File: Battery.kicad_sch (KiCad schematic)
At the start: 0 parts

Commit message: added li-pol input, start creating charging circuit
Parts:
- added J4: B2B-PH-K-S, Connector_JST:JST_PH_B2B-PH-K_1x02_P2.00mm_Vertical, symbol 0_connectors:B2B-PH-K-S
- added J5: B3B-PH-K-S, Connector_JST:JST_PH_B3B-PH-K_1x03_P2.00mm_Vertical, symbol 0_connectors:B3B-PH-K-S
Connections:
- new net +BATT: J4.1 (Pin_1), J5.1 (Pin_1)
- new net GND: J4.2 (Pin_2), J5.2 (Pin_2)
- new net NTC_BATT: J5.3 (Pin_2)
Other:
- title: (none) -> Power - Battery

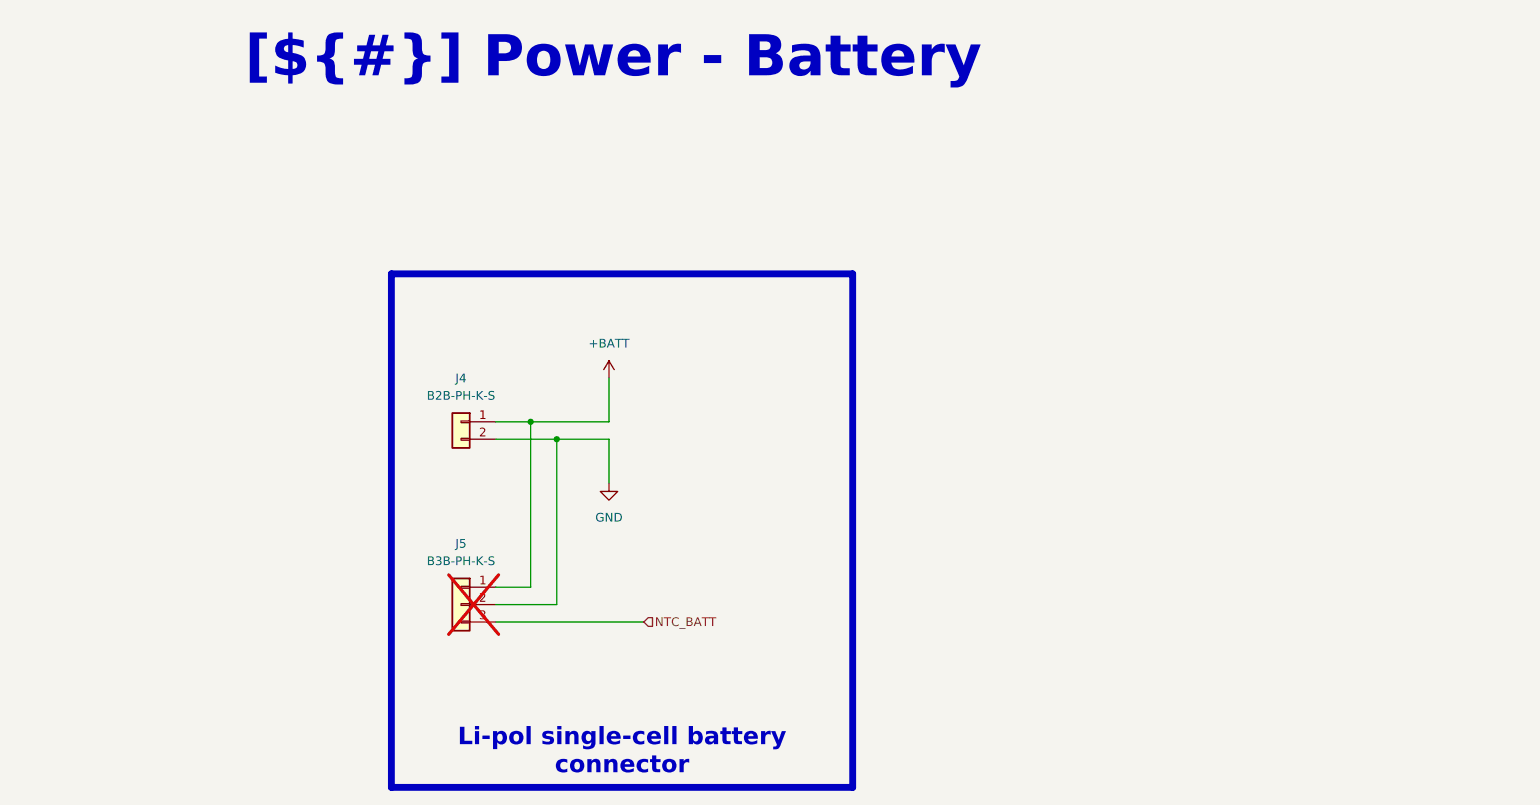
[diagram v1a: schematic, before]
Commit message: added gas guage IC for monitoring battery
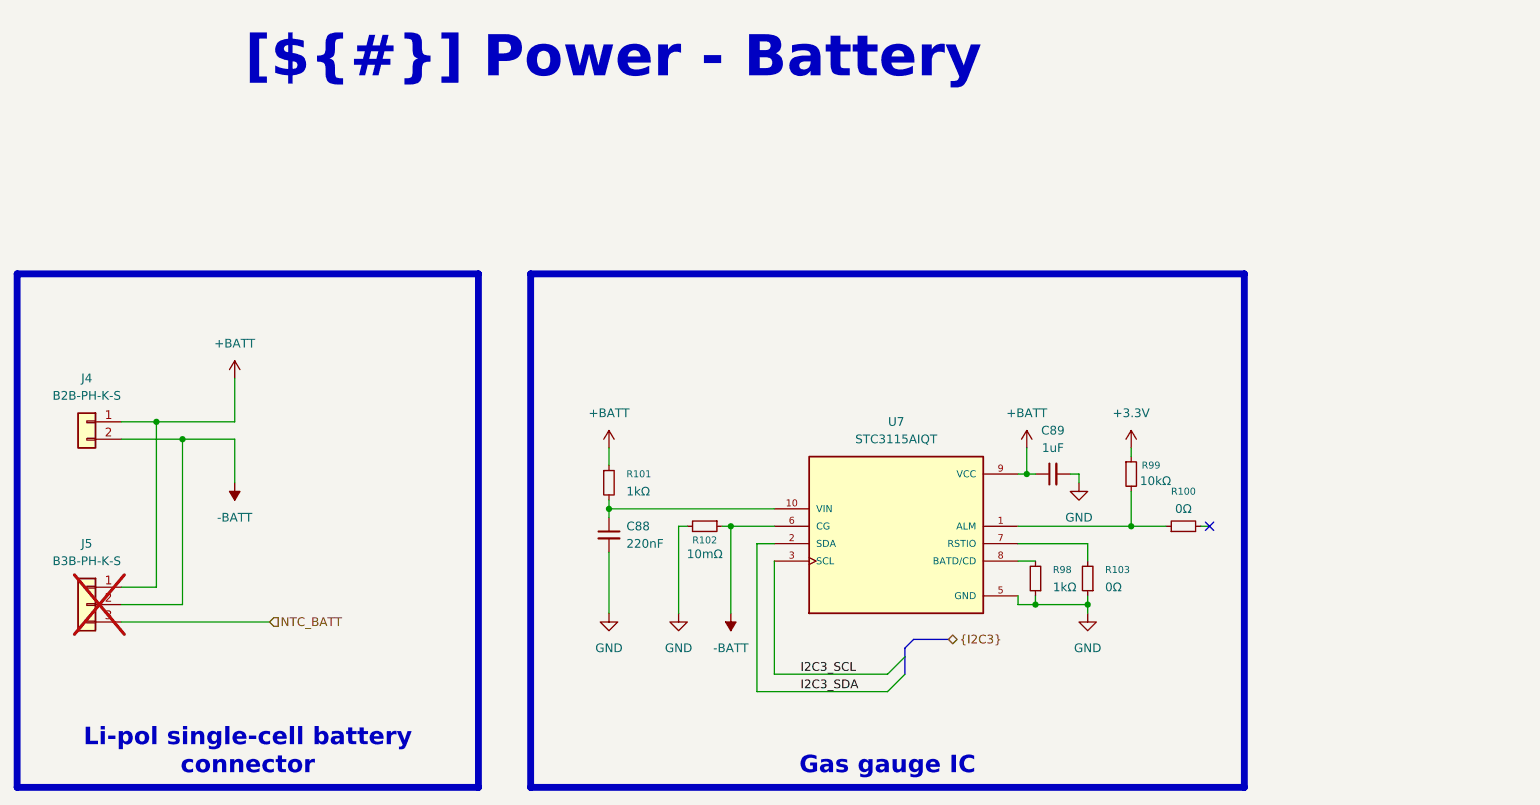
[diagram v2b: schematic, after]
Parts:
- added C88: 220nF, 0_capacitors:C_0402_1005Metric, symbol 0_capacitors:CL05B224KO5NNNC
- added C89: 1uF, 0_capacitors:C_0603_1608Metric, symbol 0_capacitors:CL10A105KB8NNNC
- added R100, R103: 0Ω, 0_resistors:R_0402_1005Metric, symbol 0_resistors:0402WGF0000TCE
- added R101, R98: 1kΩ, 0_resistors:R_0402_1005Metric, symbol 0_resistors:0402WGF1001TCE
- added R102: 10mΩ, Resistor_SMD:R_1206_3216Metric, symbol 0_resistors:FRM121WFR010TM
- added R99: 10kΩ, 0_resistors:R_0402_1005Metric, symbol 0_resistors:0402WGF1002TCE
- added U7: STC3115AIQT, 0_integrated_circuits:SON50P200X300X60-10, symbol 0_integrated_circuits:STC3115AIQT
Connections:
- net +BATT: now also C89.1, R101.1, U7.9 (VCC)
- net GND: now also C88.2, C89.2, R102.2, R103.1, R98.1, U7.5 (GND); no longer J4.2 (Pin_2), J5.2 (Pin_2)
- new net: C88.1, R101.2, U7.10 (VIN)
- new net: R100.1, R99.2, U7.1 (ALM)
- new net: R103.2, U7.7 (RSTIO)
- new net: R98.2, U7.8 (BATD/CD)
- new net +3.3V: R99.1
- new net -BATT: J4.2 (Pin_2), J5.2 (Pin_2), R102.1, U7.6 (CG)
- new net I2C3_SCL: U7.3 (SCL)
- new net I2C3_SDA: U7.2 (SDA)
- no-connect marks 0 -> 1
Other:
- moved on the sheet: J4, J5

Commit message: added fiducal markers, mounting holes, testpoints
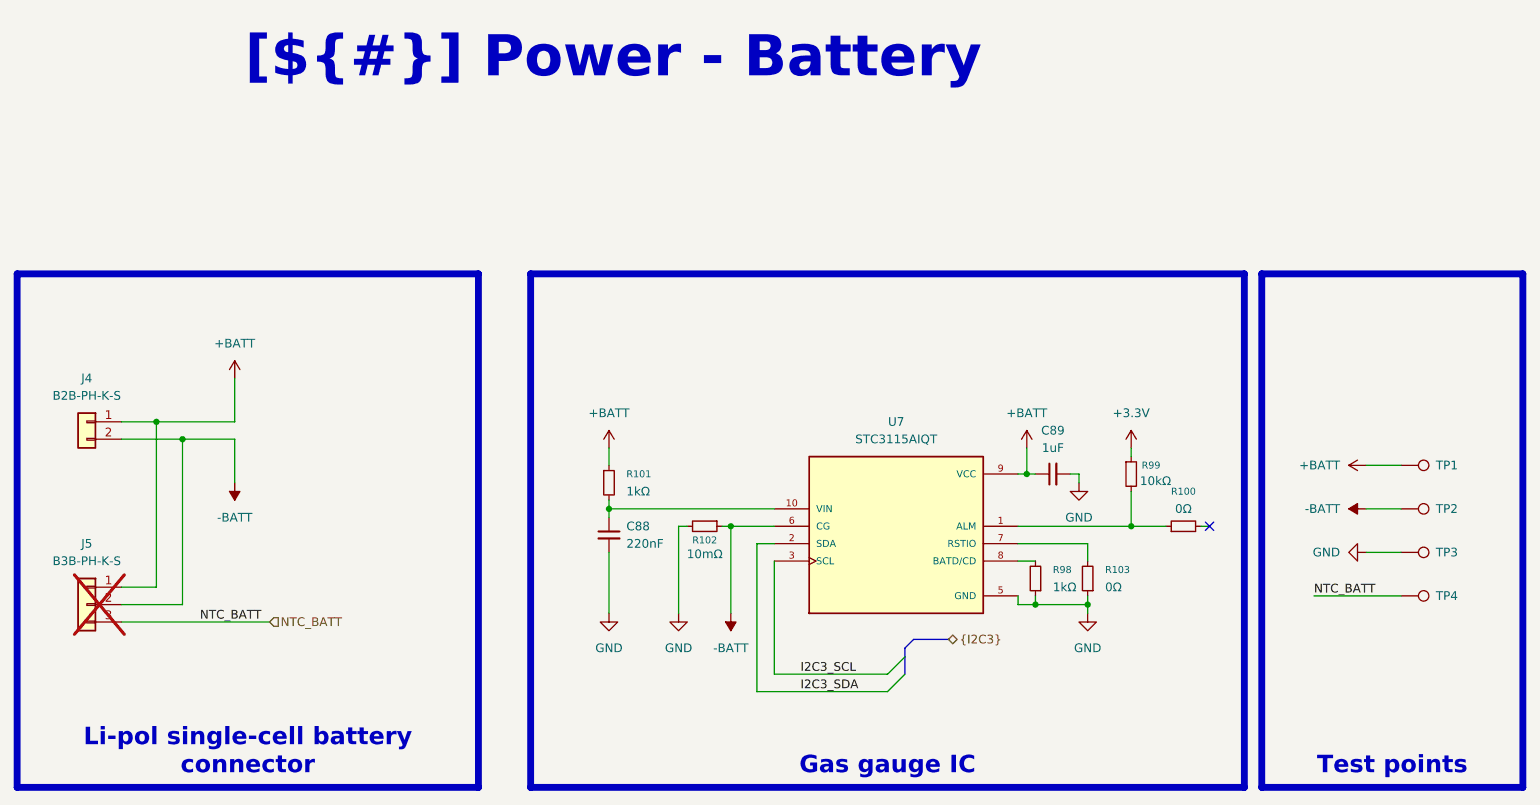
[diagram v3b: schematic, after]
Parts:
- added TP1, TP2, TP3, TP4: TestPoint, 0_pads:TestPoint_Pad_D0.4mm_Back, symbol Connector:TestPoint
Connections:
- net +BATT: now also TP1.1
- net -BATT: now also TP2.1
- net GND: now also TP3.1
- net NTC_BATT: now also TP4.1

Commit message: test points, colors, drc
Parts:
- TP1, TP2, TP3, TP4: footprint 0_pads:TestPoint_Pad_D0.4mm_Back -> 0_pads:TestPoint_Pad_D0.5mm_Back
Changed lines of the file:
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@@
 			)
 		)
-		(property "Footprint" "0_pads:TestPoint_Pad_D0.4mm_Back"
+		(property "Footprint" "0_pads:TestPoint_Pad_D0.5mm_Back"
 			(at 262.89 96.52 0)
 			(effects
@@
 			)
 		)
-		(property "Footprint" "0_pads:TestPoint_Pad_D0.4mm_Back"
+		(property "Footprint" "0_pads:TestPoint_Pad_D0.5mm_Back"
 			(at 262.89 102.87 0)
 			(effects
@@
 			)
 		)
-		(property "Footprint" "0_pads:TestPoint_Pad_D0.4mm_Back"
+		(property "Footprint" "0_pads:TestPoint_Pad_D0.5mm_Back"
 			(at 262.89 83.82 0)
 			(effects
@@
 			)
 		)
-		(property "Footprint" "0_pads:TestPoint_Pad_D0.4mm_Back"
+		(property "Footprint" "0_pads:TestPoint_Pad_D0.5mm_Back"
 			(at 262.89 90.17 0)
 			(effects

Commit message: fixing drc, generation production files test
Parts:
- added F1: 1A, symbol Device:Fuse_Small
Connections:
- net +BATT: now also F1.2; no longer J4.1 (Pin_1), J5.1 (Pin_1)
- new net: F1.1, J4.1 (Pin_1), J5.1 (Pin_1)
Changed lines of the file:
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@@
 	(wire
 		(pts
-			(xy 81.28 72.39) (xy 92.71 72.39)
+			(xy 81.28 72.39) (xy 83.82 72.39)
 		)
 		(stroke
@@
 	(wire
 		(pts
+			(xy 88.9 72.39) (xy 92.71 72.39)
+		)
+		(stroke
+			(width 0)
+			(type default)
+		)
+	)
+	(wire
+		(pts
 			(xy 147.32 83.82) (xy 147.32 85.09)
 		)
@@
 					(unit 1)
 				)
+			)
+		)
+	)
+	(symbol
+		(lib_id "Device:Fuse_Small")
+		(at 86.36 72.39 0)
+		(unit 1)
+		(exclude_from_sim no)
+		(in_bom yes)
+		(on_board yes)
+		(dnp no)
+		(fields_autoplaced yes)
+		(property "Reference" "F1"
+			(at 86.36 67.31 0)
+			(effects
+				(font
+					(size 1.27 1.27)
+				)
+			)
+		)
+		(property "Value" "1A"
+			(at 86.36 69.85 0)
+			(effects
+				(font
+					(size 1.27 1.27)
+				)
+			)
+		)
+		(property "Footprint" ""
+			(at 86.36 72.39 0)
+			(effects
+				(font
+					(size 1.27 1.27)
+				)
+				(hide yes)
+			)
+		)
+		(property "Datasheet" "~"
+			(at 86.36 72.39 0)
+			(effects
+				(font
+					(size 1.27 1.27)
+				)
+				(hide yes)
+			)
+		)
+		(property "Description" "Fuse, small symbol"
+			(at 86.36 72.39 0)
+			(effects
+				(font
+					(size 1.27 1.27)
+				)
+				(hide yes)
+			)
+		)
+		(property "Supplier 1" ""
+			(at 86.36 72.39 0)
+			(effects
+				(font
+					(size 1.27 1.27)
+				)
+				(hide yes)
+			)
+		)
+		(property "Supplier Part Number 1" "C424347"
+			(at 86.36 72.39 0)
+			(effects
+				(font
+					(size 1.27 1.27)
+				)
+				(hide yes)
+			)
+		)
+		(pin "1"
+		)
+		(pin "2"
+		)
+		(instances
+			(project ""
+				(path "/0650c7a8-acba-429c-9f8e-eec0baf0bc1c/fede4c36-00cc-4d3d-b71c-5243ba232202/44a90149-a0a1-4332-9175-9816fd2bbc11"
+					(reference "F1")
+					(unit 1)
+				)

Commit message: designator chagnes and cleanup silkscreen
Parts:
- C88: LCSC PN (none) -> C16772
- C89: LCSC PN (none) -> C15849
- F1: footprint (none) -> Fuse:Fuse_0402_1005Metric_Pad0.77x0.64mm_HandSolder
- J4: LCSC PN (none) -> C131337; Supplier 1 (none) -> JLCPCB; Supplier Part Number 1 (none) -> C131337
- J5: LCSC PN (none) -> C131339
- R100, R103: LCSC PN (none) -> C17168
- R101, R98: LCSC PN (none) -> C11702
- R102: LCSC PN (none) -> C7467248
- R99: LCSC PN (none) -> C25744
- U7: LCSC PN (none) -> C2688637
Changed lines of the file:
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@@
+			)
+		)
+		(property "LCSC PN" "C16772"
+			(at 147.32 88.9 0)
+			(effects
+				(font
+					(size 1.27 1.27)
+				)
+				(hide yes)
 			)
 		)
@@
 			)
 		)
+		(property "LCSC PN" "C17168"
+			(at 231.14 87.63 0)
+			(effects
+				(font
+					(size 1.27 1.27)
+				)
+				(hide yes)
+			)
+		)
 		(pin "1"
 		)
@@
 			)
 		)
+		(property "LCSC PN" "C15849"
+			(at 212.09 80.01 0)
+			(effects
+				(font
+					(size 1.27 1.27)
+				)
+				(hide yes)
+			)
+		)
 		(pin "2"
 		)
@@
 			)
 		)
+		(property "LCSC PN" "C11702"
+			(at 147.32 81.28 0)
+			(effects
+				(font
+					(size 1.27 1.27)
+				)
+				(hide yes)
+			)
+		)
 		(pin "1"
 		)
@@
 		)
 		(property "Supplier Part Number 1" "C25744"
+			(at 223.52 80.01 0)
+			(effects
+				(font
+					(size 1.27 1.27)
+				)
+				(hide yes)
+			)
+		)
+		(property "LCSC PN" "C25744"
 			(at 223.52 80.01 0)
 			(effects
@@
 			)
 		)
+		(property "LCSC PN" "C7467248"
+			(at 161.29 87.63 0)
+			(effects
+				(font
+					(size 1.27 1.27)
+				)
+				(hide yes)
+			)
+		)
 		(pin "1"
 		)
@@
 			)
 		)
-		(property "Footprint" ""
+		(property "Footprint" "Fuse:Fuse_0402_1005Metric_Pad0.77x0.64mm_HandSolder"
 			(at 86.36 72.39 0)
 			(effects
@@
 		)
 		(property "Supplier Part Number 1" "C424347"
+			(at 86.36 72.39 0)
+			(effects
+				(font
+					(size 1.27 1.27)
+				)
+				(hide yes)
+			)
+		)
+		(property "LCSC PN" ""
+			(at 86.36 72.39 0)
+			(effects
+				(font
+					(size 1.27 1.27)
+				)
+				(hide yes)
+			)
+		)
+		(property "TEST1" ""
 			(at 86.36 72.39 0)
 			(effects
@@
 			)
 		)
+		(property "LCSC PN" "C17168"
+			(at 217.17 95.25 0)
+			(effects
+				(font
+					(size 1.27 1.27)
+				)
+				(hide yes)
+			)
+		)
 		(pin "1"
 		)
@@
 		)
 		(property "Supplier Part Number 1" "C2688637"
+			(at 189.23 90.17 0)
+			(effects
+				(font
+					(size 1.27 1.27)
+				)
+				(hide yes)
+			)
+		)
+		(property "LCSC PN" "C2688637"
 			(at 189.23 90.17 0)
 			(effects
@@
 			)
 		)
+		(property "LCSC PN" "C131339"
+			(at 71.12 96.52 0)
+			(effects
+				(font
+					(size 1.27 1.27)
+				)
+				(hide yes)
+			)
+		)
 		(pin "1"
 		)
@@
 			)
 		)
+		(property "LCSC PN" "C11702"
+			(at 209.55 95.25 0)
+			(effects
+				(font
+					(size 1.27 1.27)
+				)
+				(hide yes)
+			)
+		)
 		(pin "1"
 		)
@@
 			(at 71.12 72.39 0)
 			(effects
+				(font
+					(size 1.27 1.27)
+				)
+				(hide yes)
+			)
+		)
+		(property "Supplier 1" "JLCPCB"
+			(at 71.12 72.39 0)
+			(effects
+				(font
+					(size 1.27 1.27)
+				)
+				(hide yes)
+			)
+		)
+		(property "LCSC PN" "C131337"
+			(at 71.12 72.39 0)
+			(effects
+				(font
+					(size 1.27 1.27)
+				)
+				(hide yes)
+			)
+		)
+		(property "Supplier Part Number 1" "C131337"
+			(at 71.12 72.39 0)
+			(effects
